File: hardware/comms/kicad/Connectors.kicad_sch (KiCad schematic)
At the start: 13 parts, among them J9 Conn_Coaxial_Small

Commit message: comms: checkpoint current KiCad design before ground station work
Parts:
- H1: renamed from H3; footprint (none) -> Ember_RF:Samtec_ESQ-126-39-G-D_2x26_P2.54mm; LCSC Part # (none) -> C7466599; MPN (none) -> ESQ-126-39-G-D; Manufacturer (none) -> Samtec; Manufacturer Part # (none) -> ESQ-126-39-G-D
- H2: renamed from H4; footprint (none) -> Ember_RF:Samtec_ESQ-126-39-G-D_2x26_P2.54mm; LCSC Part # (none) -> C7466599; MPN (none) -> ESQ-126-39-G-D; Manufacturer (none) -> Samtec; Manufacturer Part # (none) -> ESQ-126-39-G-D
- TP1: renamed from TP11; footprint (none) -> TestPoint:TestPoint_Pad_D1.0mm
- TP2: renamed from TP12; footprint (none) -> TestPoint:TestPoint_Pad_D1.0mm
- TP3: renamed from TP13; footprint (none) -> TestPoint:TestPoint_Pad_D1.0mm
- TP4: renamed from TP14; footprint (none) -> TestPoint:TestPoint_Pad_D1.0mm
- TP5: renamed from TP15; footprint (none) -> TestPoint:TestPoint_Pad_D1.0mm
- TP6: renamed from TP16; footprint (none) -> TestPoint:TestPoint_Pad_D1.0mm
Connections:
- net CAN_A_L: now reaches H1.1 (Pin_1)
- net CAN_B_L: now reaches H1.2 (Pin_2)
- net CAN_A_H: now reaches H1.3 (Pin_3)
- net CAN_B_H: now reaches H1.4 (Pin_4)
- net COMMS_IRQ: no longer names the net of H1.16 (Pin_16)
- net SPI_COMMS_CS_N: no longer names the net of H1.24 (Pin_24)
- net SPI_COMMS_MISO: no longer names the net of H1.22 (Pin_22)
- net SPI_COMMS_MOSI: no longer names the net of H1.23 (Pin_23)
- net SPI_COMMS_SCK: no longer names the net of H1.21 (Pin_21)

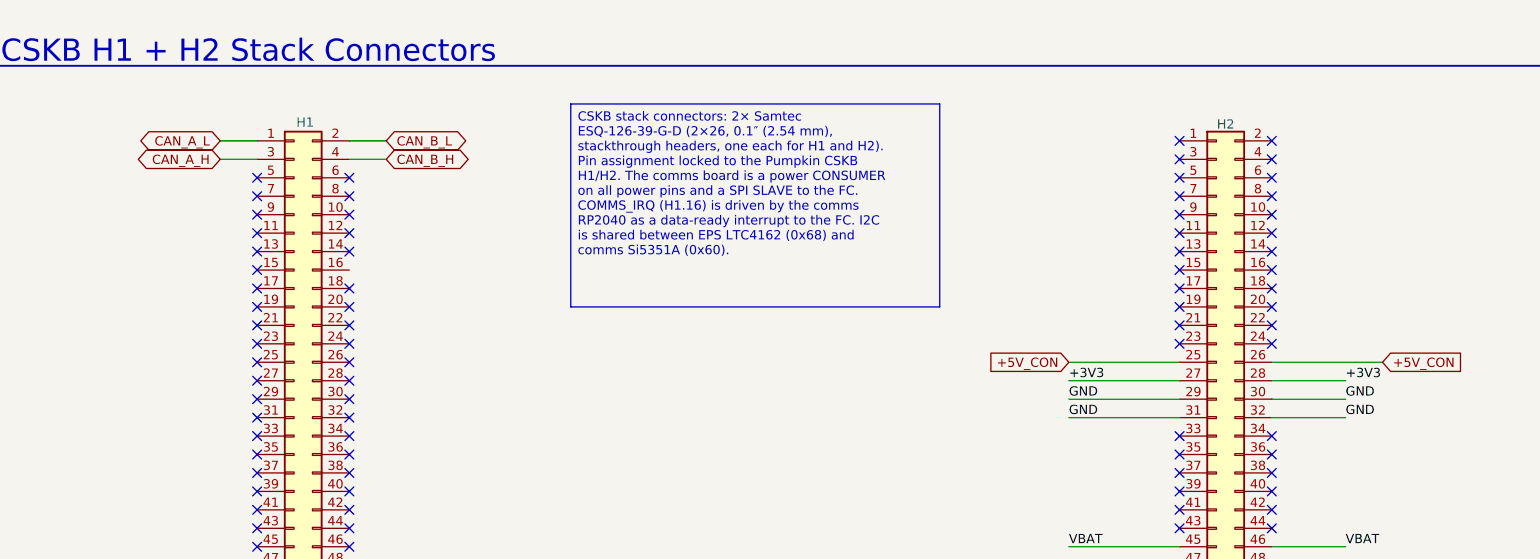
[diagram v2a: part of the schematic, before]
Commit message: Complete dual-CAN transceiver hardware prototype
Preserve the current transceiver schematics, PCB, libraries and validation evidence as a focused hardware review against main.
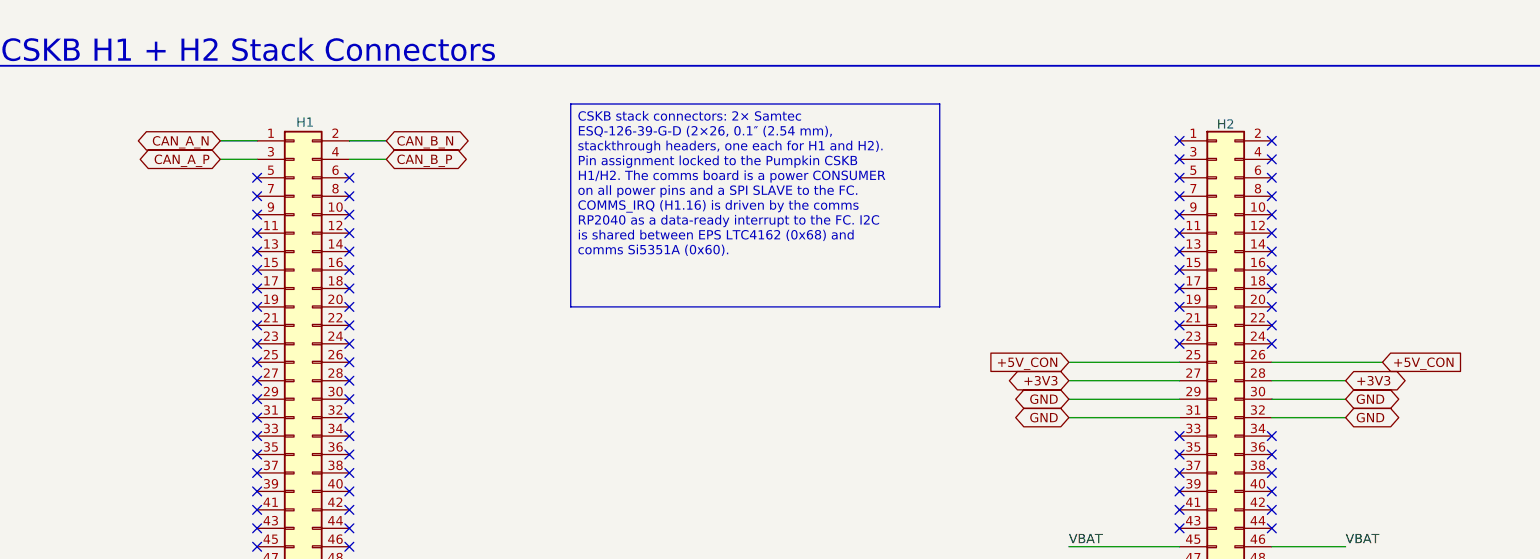
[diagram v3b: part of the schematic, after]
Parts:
- J9: LCSC Part # (none) -> C588477; MPN (none) -> 734151471; Manufacturer (none) -> Molex; Manufacturer Part # (none) -> 734151471; Qualification (none) -> Prototype selection; see verification/components/prototype_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
- TP1, TP2, TP3, TP4, TP5, TP6: Assembly (none) -> PCB feature; Assembly Notes (none) -> Bare copper test pad; no purchased component.; LCSC Part # (none) -> N/A
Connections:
- net CAN_A_H renamed CAN_A_P
- net CAN_A_L renamed CAN_A_N
- net CAN_B_H renamed CAN_B_P
- net CAN_B_L renamed CAN_B_N
- no-connect marks 89 -> 90
